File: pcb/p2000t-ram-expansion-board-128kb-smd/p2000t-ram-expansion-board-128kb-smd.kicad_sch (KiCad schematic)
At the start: 23 parts, among them J1 EXPANSION BOARD, J2 POWER, J3 TERMINAL, U1 74HC04, U2 CY62256-70PC, U3 74HC00, U4 CY62256-70PC, U5 74HC688, U6 74HC32, U7 74HC173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

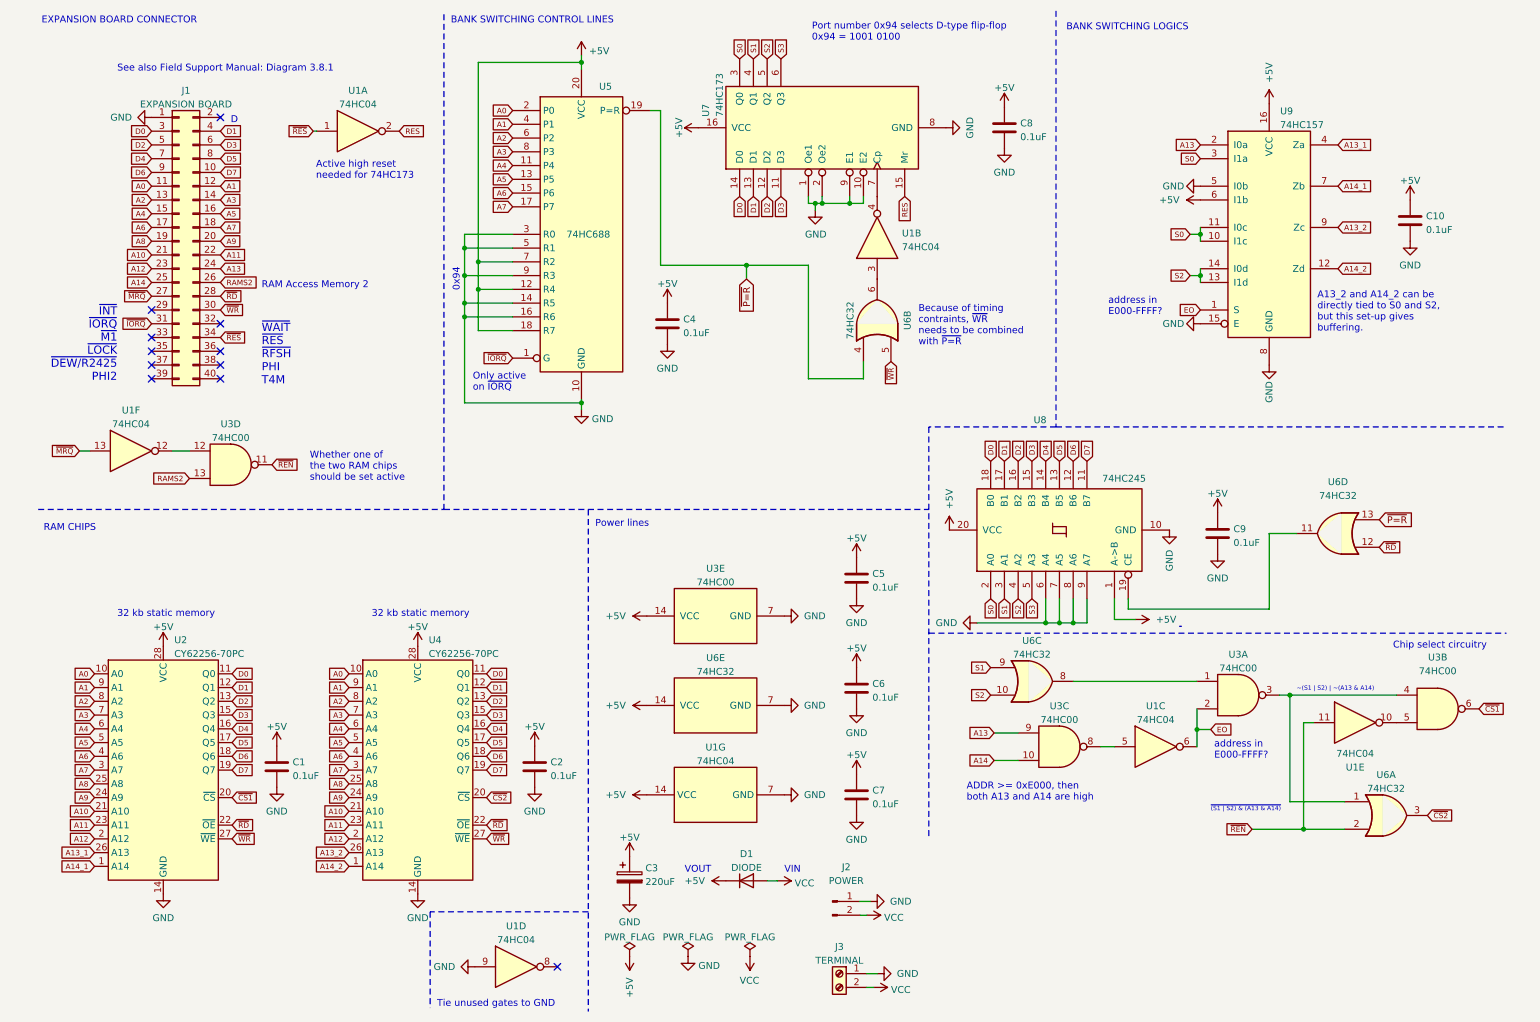
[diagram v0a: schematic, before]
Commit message: Creating 128 KiB memory expansion using SMD components (#8)
* Adding 128KiB SMD design

* Changing silk screen

* Saving schematic

* Expanding README and ram testing routines

* Revising board layout

* Adding images
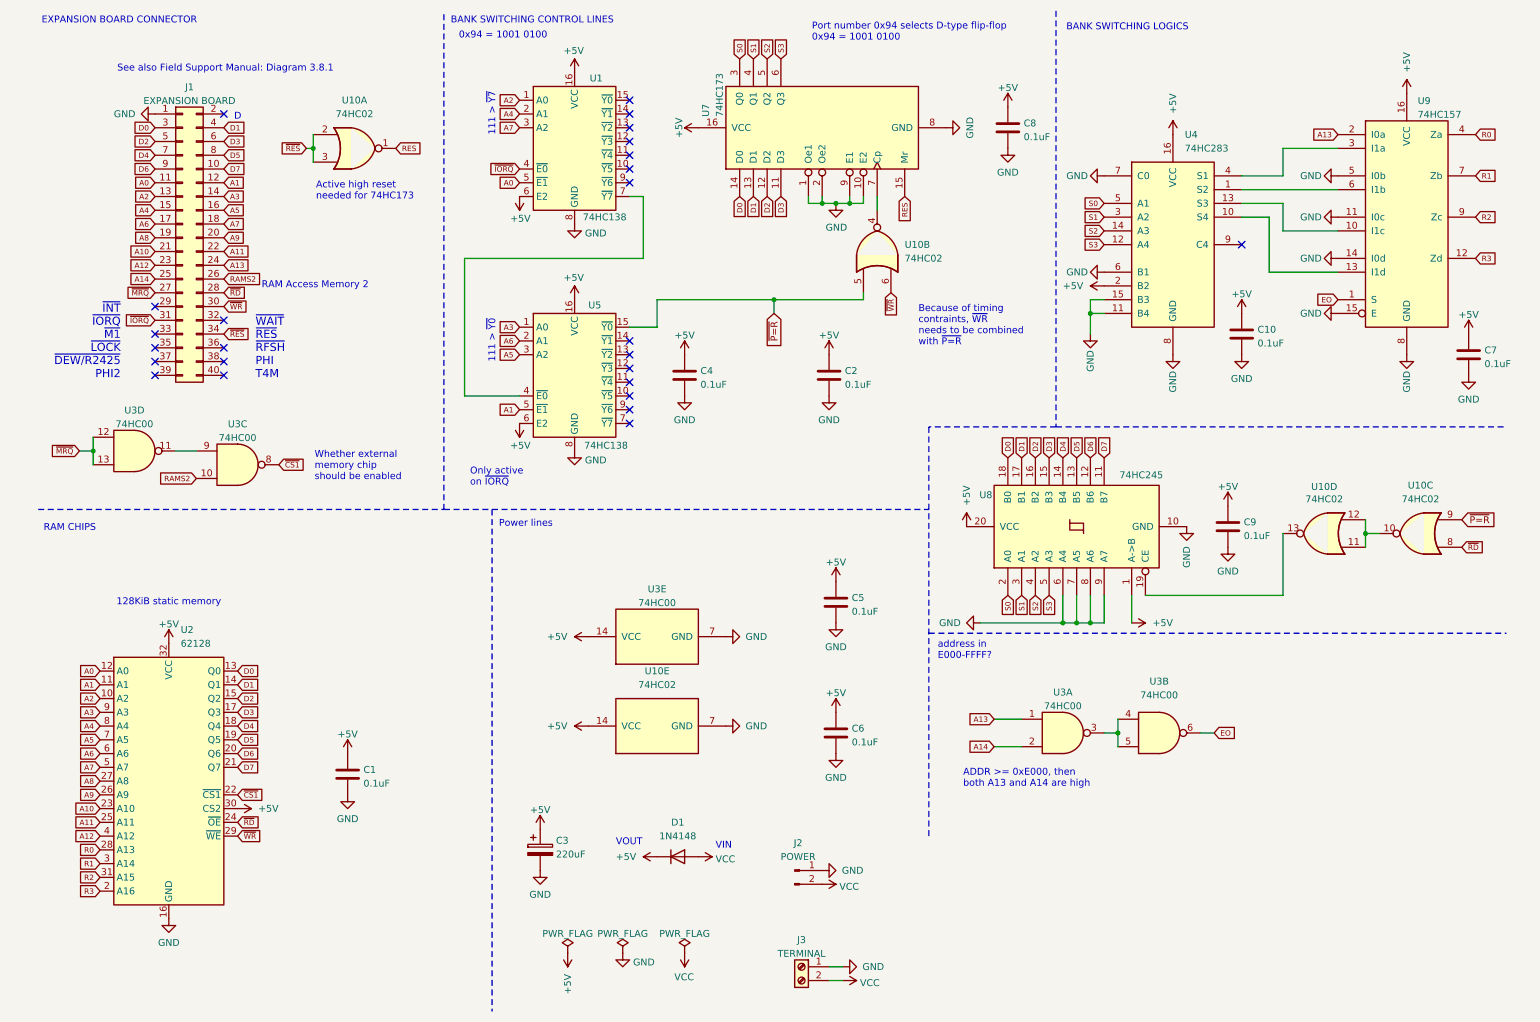
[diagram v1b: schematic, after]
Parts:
- removed J2: POWER, Connector_PinHeader_2.54mm:PinHeader_1x02_P2.54mm_Vertical, symbol Connector:Conn_01x02_Male
- removed U1: 74HC04, Package_DIP:DIP-14_W7.62mm_Socket, symbol 74xx:74HC04
- removed U2, U4: CY62256-70PC, Package_DIP:DIP-28_W15.24mm_Socket, symbol Memory_RAM:CY62256-70PC
- removed U5: 74HC688, Package_DIP:DIP-20_W7.62mm_Socket, symbol 74xx:74LS688
- removed U6: 74HC32, Package_DIP:DIP-14_W7.62mm_Socket, symbol 74xx:74LS32
- added J2: POWER, Connector_PinSocket_2.54mm:PinSocket_1x02_P2.54mm_Vertical, symbol Connector:Conn_01x02_Pin
- added U1, U5: 74HC138, Package_SO:SOIC-16_3.9x9.9mm_P1.27mm, symbol 74xx:74HC138
- added U10: 74HC02, Package_SO:SOIC-14_3.9x8.7mm_P1.27mm, symbol 74xx:74HC02
- added U2: 62128, Package_SO:SSOP-32_11.305x20.495mm_P1.27mm, symbol Memory_RAM:628128_DIP32_SSOP32
- added U4: 74HC283, Package_SO:SOIC-16_3.9x9.9mm_P1.27mm, symbol 74xx:74LS283
- C1, C10, C2, C4, C5, C6, C7, C8, C9: footprint Capacitor_THT:C_Disc_D5.0mm_W2.5mm_P5.00mm -> Capacitor_SMD:C_0805_2012Metric_Pad1.18x1.45mm_HandSolder; LCSC Part # (none) -> C126469
- D1: value DIODE -> 1N4148
- U3: footprint Package_DIP:DIP-14_W7.62mm_Socket -> Package_SO:SOIC-14_3.9x8.7mm_P1.27mm; LCSC Part # (none) -> C699445
- U7: footprint Package_DIP:DIP-16_W7.62mm_Socket -> Package_SO:SOIC-16_3.9x9.9mm_P1.27mm; LCSC Part # (none) -> C546651
- U8: footprint Package_DIP:DIP-20_W7.62mm_Socket -> Package_SO:SOIC-20W_7.5x12.8mm_P1.27mm; LCSC Part # (none) -> C5625
- U9: footprint Package_DIP:DIP-16_W7.62mm_Socket -> Package_SO:SOIC-16_3.9x9.9mm_P1.27mm; LCSC Part # (none) -> C6823
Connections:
- net +5V: now also U1.16 (VCC), U1.6 (E2), U10.14 (VCC), U2.30 (CS2), U2.32 (VCC), U4.16 (VCC), U4.2 (B2), U5.16 (VCC), U5.6 (E2); no longer U9.6 (I1b)
- net A0: now also U1.5 (~{E1}), U2.12 (A0)
- net A1: now also U2.11 (A1), U5.5 (~{E1})
- net A10: now also U2.23 (A10)
- net A11: now also U2.25 (A11)
- net A12: now also U2.4 (A12)
- net A13: now also U3.1; no longer U3.9
- net A14: now also U3.2; no longer U3.10
- net A2: now also U1.1 (A0), U2.10 (A2)
- net A3: now also U2.9 (A3), U5.1 (A0)
- net A4: now also U1.2 (A1), U2.8 (A4)
- net A5: now also U2.7 (A5), U5.3 (A2)
- net A6: now also U2.6 (A6), U5.2 (A1)
- net A7: now also U1.3 (A2), U2.5 (A7)
- net A8: now also U2.27 (A8)
- net A9: now also U2.26 (A9)
- net D0: now also U2.13 (Q0)
- net D1: now also U2.14 (Q1)
- net D2: now also U2.15 (Q2)
- net D3: now also U2.17 (Q3)
- net D4: now also U2.18 (Q4)
- net D5: now also U2.19 (Q5)
- net D6: now also U2.20 (Q6)
- net D7: now also U2.21 (Q7)
- net EO: now also U3.6; no longer U3.2
- net GND: now also U9.11 (I0c), U9.14 (I0d), J2.1 (Pin_1), U1.8 (GND), U10.7 (GND), U2.16 (GND), U4.11 (B4), U4.15 (B3), U4.6 (B1), U4.7 (C0), U4.8 (GND), U5.8 (GND)
- net RAMS2: now also U3.10; no longer U3.13
- net RES: now also U10.1
- net S0: now also U4.5 (A1); no longer U9.10 (I1c), U9.11 (I0c), U9.3 (I1a)
- net S1: now also U4.3 (A2)
- net S2: now also U4.14 (A3); no longer U9.13 (I1d), U9.14 (I0d)
- net S3: now also U4.12 (A4)
- net VCC: now also J2.2 (Pin_2)
- net ~{CS1}: now also U3.8, U2.22 (~{CS1}); no longer U3.6
- net ~{IORQ}: now also U1.4 (~{E0})
- net ~{MRQ}: now also U3.12, U3.13
- net ~{P=R}: now also U10.5, U10.9, U5.15 (~{Y0})
- net ~{RD}: now also U10.8, U2.24 (~{OE})
- net ~{RES}: now also U10.2, U10.3
- net ~{WR}: now also U10.6, U2.29 (~{WE})
- net at U3.3, U3.4: now also U3.5
- net at U7.7 (Cp): now also U10.4
- net at U8.19 (CE): now also U10.13
- net A13_1 renamed R0
- net R0: now also U2.28 (A13)
- net A13_2 renamed R2
- net R2: now also U2.31 (A15)
- net A14_1 renamed R1
- net R1: now also U2.3 (A14)
- net A14_2 renamed R3
- net R3: now also U2.2 (A16)
- net ~{REN}: no longer names the net of U3.11
- net ~{REN}: now also U3.9
- new net: U4.1 (S2), U9.6 (I1b)
- new net: U4.10 (S4), U9.13 (I1d)
- new net: U4.13 (S3), U9.10 (I1c)
- new net: U4.4 (S1), U9.3 (I1a)
- new net: U10.10, U10.11, U10.12
- new net: U1.7 (~{Y7}), U5.4 (~{E0})
- no-connect marks 11 -> 25
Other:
- note added: "0x94 = 1001 0100"
- note added: "111 > ~{Y0}"
- note added: "111 > ~{Y7}"
- note added: "128KiB static memory"
- note added: "Whether external memory chip should be enabled"
- note removed: "0x94"
- note removed: "32 kb static memory"
- note removed: "A13_2 and A14_2 can be directly tied to S0 and S2, but this set-up gives buffering."
- note removed: "Chip select circuitry"
- note removed: "Tie unused gates to GND"
- note removed: "Whether one of the two RAM chips should be set active"
- note removed: "~(S1 | S2) | ~(A13 & A14)"
- note removed: "~{(S1 | S2) & (A13 & A14)}"
- title: Philips P2000T 64kb memory expansion board -> Philips P2000T 128KiB memory expansion board (SMD)
- moved on the sheet: C1, C10, C3, C4, C5, C6, C7, C8, C9, D1, J1, J3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

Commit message: Initial commit CPLD-based RAM expansion
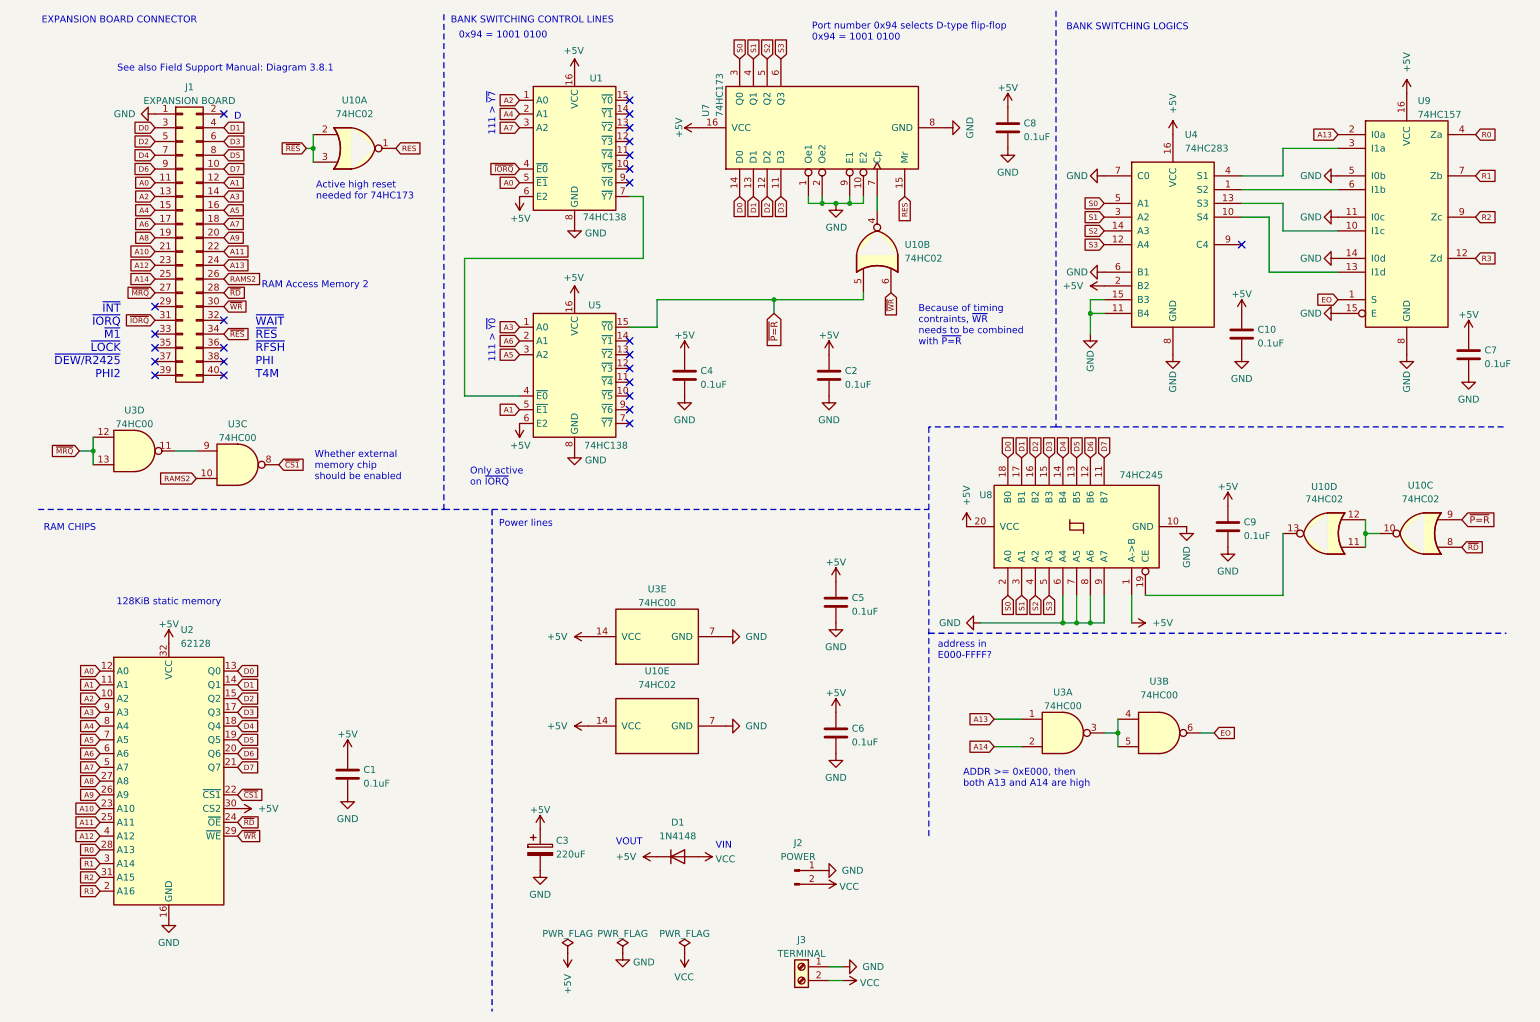
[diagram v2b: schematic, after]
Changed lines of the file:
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@@
 (kicad_sch
-	(version 20231120)
+	(version 20250114)
 	(generator "eeschema")
-	(generator_version "8.0")
+	(generator_version "9.0")
 	(paper "A4")
 	(title_block
@@
 		(rev "0")
 	)
+	(text "VIN"
+		(exclude_from_sim no)
+		(at 137.795 167.64 0)
+		(effects
+			(font
+				(size 1.27 1.27)
+			)
+			(justify left bottom)
+		)
+	)
+	(text "EXPANSION BOARD CONNECTOR"
+		(exclude_from_sim no)
+		(at 13.335 15.24 0)
+		(effects
+			(font
+				(size 1.27 1.27)
+			)
+			(justify left bottom)
+		)
+	)
+	(text "VOUT"
+		(exclude_from_sim no)
+		(at 119.38 167.005 0)
+		(effects
+			(font
+				(size 1.27 1.27)
+			)
+			(justify left bottom)
+		)
+	)
+	(text "0x94 = 1001 0100"
+		(exclude_from_sim no)
+		(at 98.552 17.272 0)
+		(effects
+			(font
+				(size 1.27 1.27)
+			)
+		)
+	)
+	(text "~{INT}\n~{IORQ}\n~{M1}\n~{LOCK}\n~{DEW/R2425}\nPHI2"
+		(exclude_from_sim no)
+		(at 27.94 80.772 0)
+		(effects
+			(font
+				(size 1.5 1.5)
+			)
+			(justify right bottom)
+		)
+	)
+	(text "D"
+		(exclude_from_sim no)
+		(at 48.895 33.02 0)
+		(effects
+			(font
+				(size 1.27 1.27)
+			)
+			(justify left bottom)
+		)
+	)
+	(text "Only active\non ~{IORQ}"
+		(exclude_from_sim no)
+		(at 92.456 100.584 0)
+		(effects
+			(font
+				(size 1.27 1.27)
+			)
+			(justify left bottom)
+		)
+	)
+	(text "RAM Access Memory 2"
+		(exclude_from_sim no)
+		(at 53.975 64.135 0)
+		(effects
+			(font
+				(size 1.27 1.27)
+			)
+			(justify left bottom)
+		)
+	)
+	(text "111 > ~{Y0}"
+		(exclude_from_sim no)
+		(at 96.52 73.66 90)
+		(effects
+			(font
+				(size 1.27 1.27)
+			)
+		)
+	)
+	(text "address in\nE000-FFFF?"
+		(exclude_from_sim no)
+		(at 178.816 132.588 0)
+		(effects
+			(font
+				(size 1.27 1.27)
+			)
+			(justify left bottom)
+		)
+	)
+	(text "111 > ~{Y7}"
+		(exclude_from_sim no)
+		(at 96.52 31.75 90)
+		(effects
+			(font
+				(size 1.27 1.27)
+			)
+		)
+	)
+	(text "Because of timing\ncontraints, ~{WR}\nneeds to be combined\nwith ~{P=R}"
+		(exclude_from_sim no)
+		(at 175.26 74.676 0)
+		(effects
+			(font
+				(size 1.27 1.27)
+			)
+			(justify left bottom)
+		)
+	)
+	(text "BANK SWITCHING LOGICS"
+		(exclude_from_sim no)
+		(at 202.565 16.51 0)
+		(effects
+			(font
+				(size 1.27 1.27)
+			)
+			(justify left bottom)
+		)
+	)
+	(text "RAM CHIPS"
+		(exclude_from_sim no)
+		(at 13.716 108.966 0)
+		(effects
+			(font
+				(size 1.27 1.27)
+			)
+			(justify left bottom)
+		)
+	)
+	(text "See also Field Support Manual: Diagram 3.8.1"
+		(exclude_from_sim no)
+		(at 27.305 24.13 0)
+		(effects
+			(font
+				(size 1.27 1.27)
+			)
+			(justify left bottom)
+		)
+	)
+	(text "Power lines"
+		(exclude_from_sim no)
+		(at 97.79 108.204 0)
+		(effects
+			(font
+				(size 1.27 1.27)
+			)
+			(justify left bottom)
+		)
+	)
+	(text "BANK SWITCHING CONTROL LINES"
+		(exclude_from_sim no)
+		(at 88.9 15.24 0)
+		(effects
+			(font
+				(size 1.27 1.27)
+			)
+			(justify left bottom)
+		)
+	)
+	(text "128KiB static memory"
+		(exclude_from_sim no)
+		(at 27.178 122.682 0)
+		(effects
+			(font
+				(size 1.27 1.27)
+			)
+			(justify left bottom)
+		)
+	)
+	(text "ADDR >= 0xE000, then \nboth A13 and A14 are high"
+		(exclude_from_sim no)
+		(at 183.515 156.21 0)
+		(effects
+			(font
+				(size 1.27 1.27)
+			)
+			(justify left bottom)
+		)
+	)
+	(text "~{WAIT}\n~{RES}\n~{RFSH}\nPHI\nT4M"
+		(exclude_from_sim no)
+		(at 52.832 80.772 0)
+		(effects
+			(font
+				(size 1.5 1.5)
+			)
+			(justify left bottom)
+		)
+	)
+	(text "Active high reset\nneeded for 74HC173"
+		(exclude_from_sim no)
+		(at 64.008 47.752 0)
+		(effects
+			(font
+				(size 1.27 1.27)
+			)
+			(justify left bottom)
+		)
+	)
+	(text "Whether external \nmemory chip\nshould be enabled"
+		(exclude_from_sim no)
+		(at 63.754 99.568 0)
+		(effects
+			(font
+				(size 1.27 1.27)
+			)
+			(justify left bottom)
+		)
+	)
+	(text "Port number 0x94 selects D-type flip-flop\n0x94 = 1001 0100"
+		(exclude_from_sim no)
+		(at 155.575 18.415 0)
+		(effects
+			(font
+				(size 1.27 1.27)
+			)
+			(justify left bottom)
+		)
+	)
 	(junction
 		(at 160.02 48.26)
@@
 		)
 	)
-	(text "VIN"
-		(exclude_from_sim no)
-		(at 137.795 167.64 0)
-		(effects
-			(font
-				(size 1.27 1.27)
-			)
-			(justify left bottom)
-		)
-	)
-	(text "EXPANSION BOARD CONNECTOR"
-		(exclude_from_sim no)
-		(at 13.335 15.24 0)
-		(effects
-			(font
-				(size 1.27 1.27)
-			)
-			(justify left bottom)
-		)
-	)
-	(text "VOUT"
-		(exclude_from_sim no)
-		(at 119.38 167.005 0)
-		(effects
-			(font
-				(size 1.27 1.27)
-			)
-			(justify left bottom)
-		)
-	)
-	(text "0x94 = 1001 0100"
-		(exclude_from_sim no)
-		(at 98.552 17.272 0)
-		(effects
-			(font
-				(size 1.27 1.27)
-			)
-		)
-	)
-	(text "~{INT}\n~{IORQ}\n~{M1}\n~{LOCK}\n~{DEW/R2425}\nPHI2"
-		(exclude_from_sim no)
-		(at 27.94 80.772 0)
-		(effects
-			(font
-				(size 1.5 1.5)
-			)
-			(justify right bottom)
-		)
-	)
-	(text "D"
-		(exclude_from_sim no)
-		(at 48.895 33.02 0)
-		(effects
-			(font
-				(size 1.27 1.27)
-			)
-			(justify left bottom)
-		)
-	)
-	(text "Only active\non ~{IORQ}"
-		(exclude_from_sim no)
-		(at 92.456 100.584 0)
-		(effects
-			(font
-				(size 1.27 1.27)
-			)
-			(justify left bottom)
-		)
-	)
-	(text "RAM Access Memory 2"
-		(exclude_from_sim no)
-		(at 53.975 64.135 0)
-		(effects
-			(font
-				(size 1.27 1.27)
-			)
-			(justify left bottom)
-		)
-	)
-	(text "111 > ~{Y0}"
-		(exclude_from_sim no)
-		(at 96.52 73.66 90)
-		(effects
-			(font
-				(size 1.27 1.27)
-			)
-		)
-	)
-	(text "address in\nE000-FFFF?"
-		(exclude_from_sim no)
-		(at 178.816 132.588 0)
-		(effects
-			(font
-				(size 1.27 1.27)
-			)
-			(justify left bottom)
-		)
-	)
-	(text "111 > ~{Y7}"
-		(exclude_from_sim no)
-		(at 96.52 31.75 90)
-		(effects
-			(font
-				(size 1.27 1.27)
-			)
-		)
-	)
-	(text "Because of timing\ncontraints, ~{WR}\nneeds to be combined\nwith ~{P=R}"
-		(exclude_from_sim no)
-		(at 175.26 74.676 0)
-		(effects
-			(font
-				(size 1.27 1.27)
-			)
-			(justify left bottom)
-		)
-	)
-	(text "BANK SWITCHING LOGICS"
-		(exclude_from_sim no)
-		(at 202.565 16.51 0)
-		(effects
-			(font
-				(size 1.27 1.27)
-			)
-			(justify left bottom)
-		)
-	)
-	(text "RAM CHIPS"
-		(exclude_from_sim no)
-		(at 13.716 108.966 0)
-		(effects
-			(font
-				(size 1.27 1.27)
-			)
-			(justify left bottom)
-		)
-	)
-	(text "See also Field Support Manual: Diagram 3.8.1"
-		(exclude_from_sim no)
-		(at 27.305 24.13 0)
-		(effects
-			(font
-				(size 1.27 1.27)
-			)
-			(justify left bottom)
-		)
-	)
-	(text "Power lines"
-		(exclude_from_sim no)
-		(at 97.79 108.204 0)
-		(effects
-			(font
-				(size 1.27 1.27)
-			)
-			(justify left bottom)
-		)
-	)
-	(text "BANK SWITCHING CONTROL LINES"
-		(exclude_from_sim no)
-		(at 88.9 15.24 0)
-		(effects
-			(font
-				(size 1.27 1.27)
-			)
-			(justify left bottom)
-		)
-	)
-	(text "128KiB static memory"
-		(exclude_from_sim no)
-		(at 27.178 122.682 0)
-		(effects
-			(font
-				(size 1.27 1.27)
-			)
-			(justify left bottom)
-		)
-	)
-	(text "ADDR >= 0xE000, then \nboth A13 and A14 are high"
-		(exclude_from_sim no)
-		(at 183.515 156.21 0)
-		(effects
-			(font
-				(size 1.27 1.27)
-			)
-			(justify left bottom)
-		)
-	)
-	(text "~{WAIT}\n~{RES}\n~{RFSH}\nPHI\nT4M"
-		(exclude_from_sim no)
-		(at 52.832 80.772 0)
-		(effects
-			(font
-				(size 1.5 1.5)
-			)
-			(justify left bottom)
-		)
-	)
-	(text "Active high reset\nneeded for 74HC173"
-		(exclude_from_sim no)
-		(at 64.008 47.752 0)
-		(effects
-			(font
-				(size 1.27 1.27)
-			)
-			(justify left bottom)
-		)
-	)
-	(text "Whether external \nmemory chip\nshould be enabled"
-		(exclude_from_sim no)
-		(at 63.754 99.568 0)
-		(effects
-			(font
-				(size 1.27 1.27)
-			)
-			(justify left bottom)
-		)
-	)
-	(text "Port number 0x94 selects D-type flip-flop\n0x94 = 1001 0100"
-		(exclude_from_sim no)
-		(at 155.575 18.415 0)
-		(effects
-			(font
-				(size 1.27 1.27)
-			)
-			(justify left bottom)
-		)
-	)
 	(global_label "~{P=R}"
 		(shape input)
@@
 		)
 	)
+	(embedded_fonts no)
 )
